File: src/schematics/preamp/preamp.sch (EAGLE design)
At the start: 35 parts

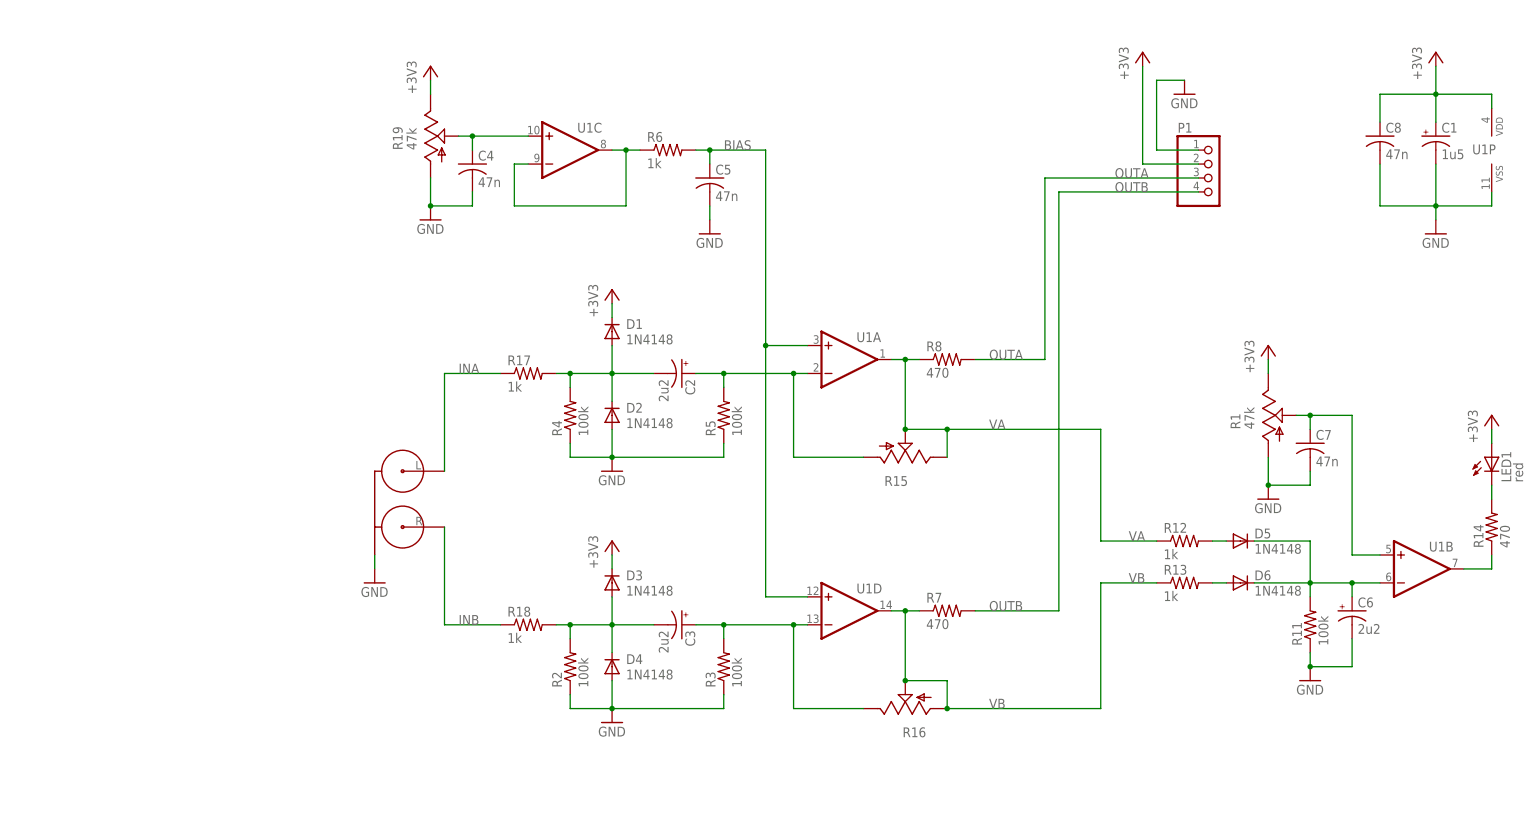
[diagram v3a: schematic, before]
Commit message: Window comparator for preamp calibration
The positive voltage reference for opamps is now reduced to a simple
potentiometer, sithout impedance decoupling (not strictly needed).

Two opamps are used as comparators for windowing of the rectified input
signals. This way it is possible to warn the user if the signal is too low
like before (bad comparator results) and also if the signal is too strong,
thus leading to a potentially wring duty cycle of the squared wave.

Andrea Zoppi
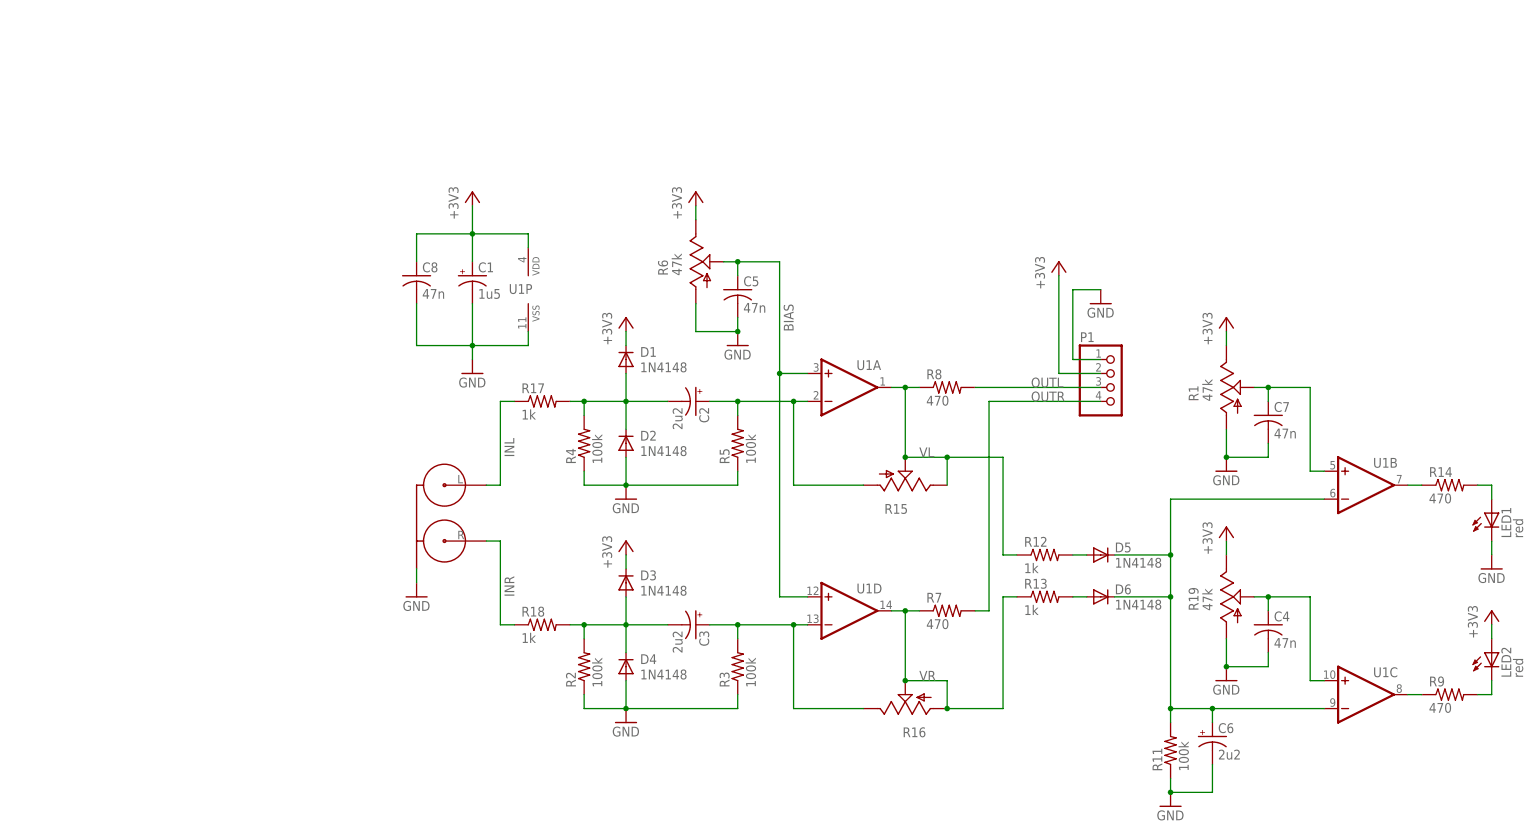
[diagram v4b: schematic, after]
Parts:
- added LED2: red, led:LED3MM
- added R9: 470, rcl:R-US_0204/5
- R6: value 1k -> 47k; device rcl:R-US_0204/5 -> pot:TRIM_US-PT-10S
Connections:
- net INA renamed INL
- net INB renamed INR
- net OUTA renamed OUTL
- net OUTB renamed OUTR
- net VA renamed VL
- net VB renamed VR
- removed net N$14: R19.A
- new net N$2: R9.1, U1C.OUT
- net +3V3: now also LED2.A, R6.E; no longer LED1.A
- net BIAS: now also R6.S; no longer R6.2
- net GND: now also LED1.C, R19.A, R6.A
- net N$12: now also LED2.C, R9.2; no longer LED1.C, R14.2
- net N$4: now also U1C.-IN
- net N$7: now also LED1.A, R14.2; no longer R6.1, U1C.-IN, U1C.OUT
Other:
- moved on the sheet: C1, C2, C3, C4, C5, C6, C7, C8, D1, D2, D3, D4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
